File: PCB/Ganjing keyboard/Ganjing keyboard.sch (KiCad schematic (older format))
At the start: 166 parts, among them J1 AVR-ISP-6, J2 Conn_01x04, SW1 Rotary_Encoder_Switch, U1 ATmega32A-PU, Y1 Crystal

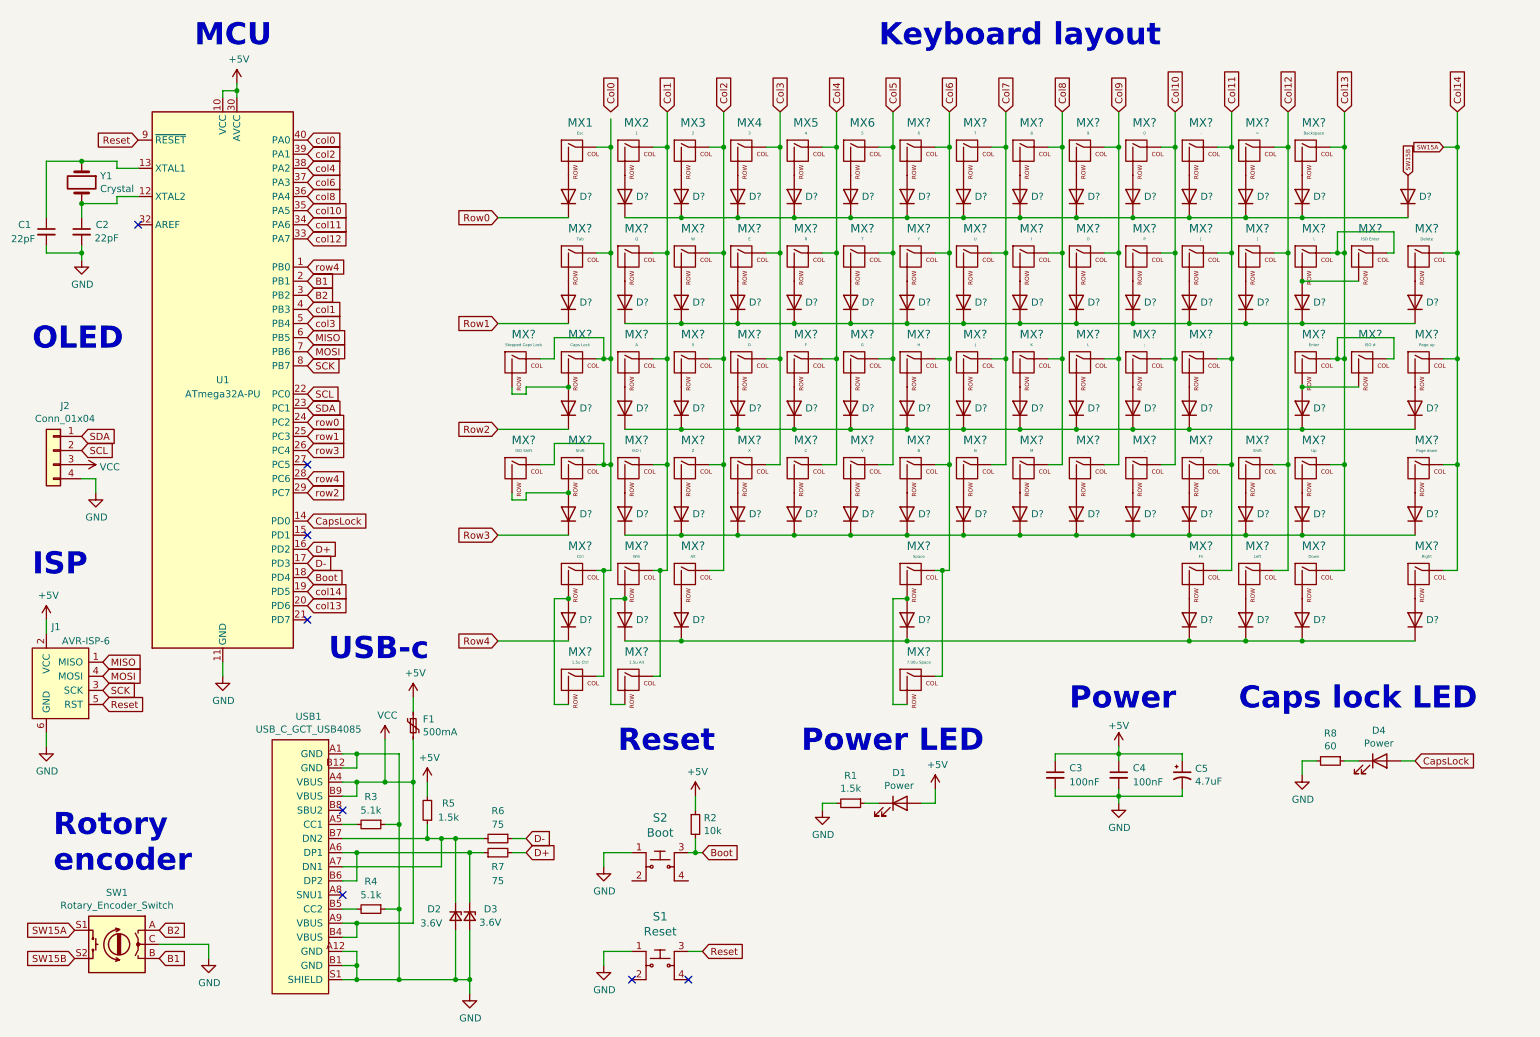
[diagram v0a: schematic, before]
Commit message: Updated schematic with reference values
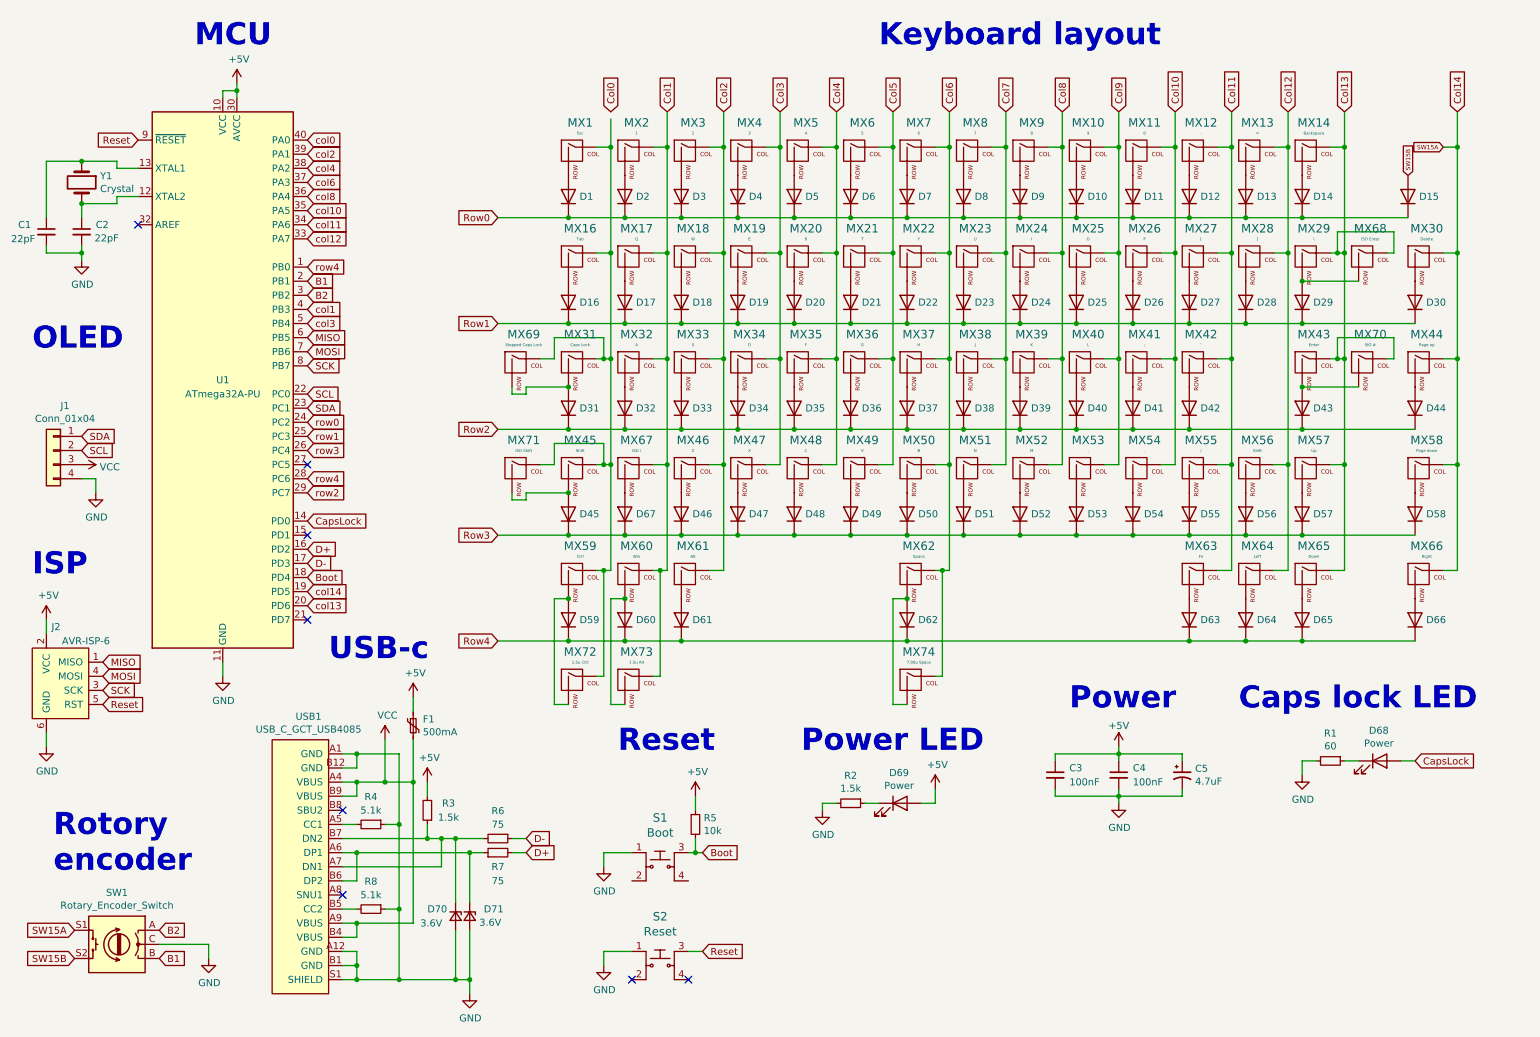
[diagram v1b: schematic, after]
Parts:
- gave numbers to parts that had none: 134
- renumbered D4 to D68, D1 to D69, D2 to D70, D3 to D71, J2 to J1, J1 to J2, R8 to R1, R1 to R2, R5 to R3, R3 to R4, R2 to R5, R4 to R8, S2 to S1, S1 to S2
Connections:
- net Row0: now also D10.1 (K), D11.1 (K), D12.1 (K), D13.1 (K), D14.1 (K), D15.1 (K), D2.1 (K), D3.1 (K), D4.1 (K), D5.1 (K), D6.1 (K), D7.1 (K), D8.1 (K), D9.1 (K)
- net Row1: now also D17.1 (K), D18.1 (K), D19.1 (K), D20.1 (K), D21.1 (K), D22.1 (K), D23.1 (K), D24.1 (K), D25.1 (K), D26.1 (K), D27.1 (K), D28.1 (K), D29.1 (K), D30.1 (K)
- net Row2: now also D32.1 (K), D33.1 (K), D34.1 (K), D35.1 (K), D36.1 (K), D37.1 (K), D38.1 (K), D39.1 (K), D40.1 (K), D41.1 (K), D42.1 (K), D43.1 (K), D44.1 (K)
- net Row3: now also D46.1 (K), D47.1 (K), D48.1 (K), D49.1 (K), D50.1 (K), D51.1 (K), D52.1 (K), D53.1 (K), D54.1 (K), D55.1 (K), D56.1 (K), D57.1 (K), D58.1 (K), D67.1 (K)
- net Row4: now also D60.1 (K), D61.1 (K), D62.1 (K), D63.1 (K), D64.1 (K), D65.1 (K), D66.1 (K)

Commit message: Added part numbers, links, and datasheets to all symbols, as well as changing the 60 ohm resistor to 62 ohm. All symbols now have associated footprints
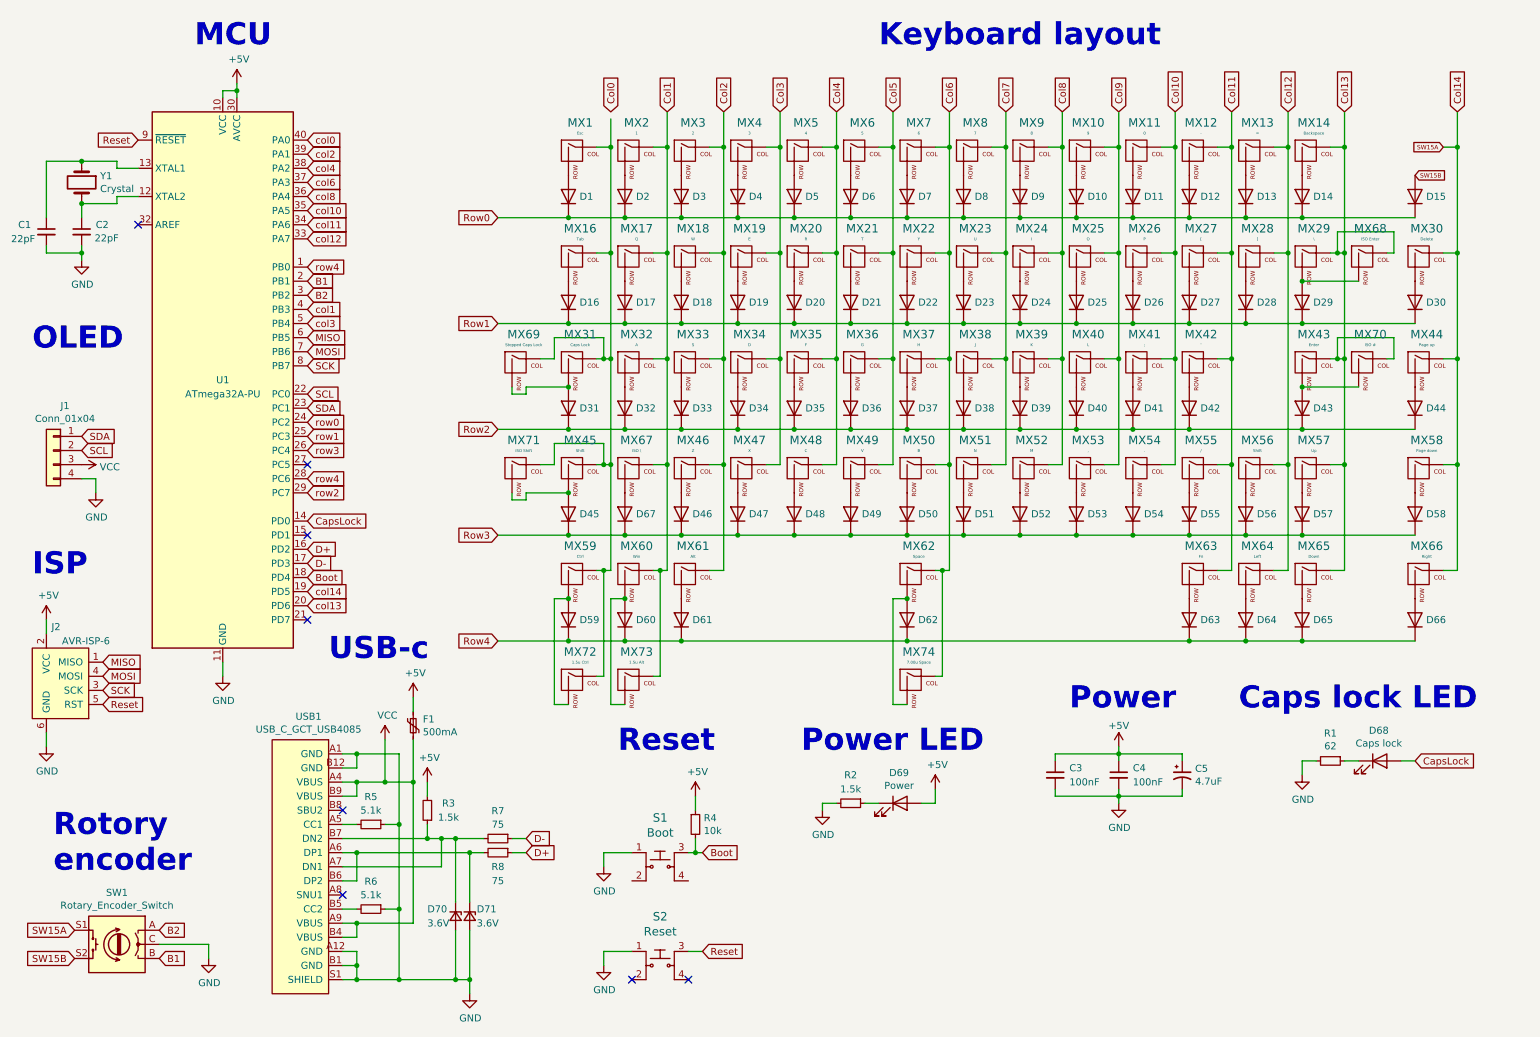
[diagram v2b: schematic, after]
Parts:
- removed R7: 75, symbol Device:R_Small
- added R6: 5.1k, Resistor_THT:R_Axial_DIN0204_L3.6mm_D1.6mm_P5.08mm_Horizontal, symbol Device:R_Small
- C1, C2: footprint (none) -> Keyboard:C_Disc_D3.0mm_W1.6mm_P2.50mm; Digikey # (none) -> 490-11879-ND; Digikey link (none) -> https://www.digikey.ca/en/products/detail/murata-electronic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
- C3, C4: footprint (none) -> Keyboard:C_Disc_D4.3mm_W1.9mm_P5.00mm; Digikey # (none) -> https://www.digikey.ca/en/products/detail/murata-electronic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; Digikey link (none) -> https://www.digikey.ca/en/products/detail/murata-electronic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
- C5: footprint (none) -> Keyboard:CP_Radial_D4.0mm_P1.50mm; Mouser # (none) -> 647-UMT1H4R7MDD1TP; Mouser link (none) -> https://www.mouser.com/ProductDetail/Nichicon/UMT1H4R7MDD1T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
- D1, D10, D11, D12, D13, D14, D15, D16, D17, D18, D19, D2, D20, D21, D22, D23, D24, D25, D26, D27, D28, D29, D3, D30, D31, D32, D33, D34, D35, D36, D37, D38, D39, D4, D40, D41, D42, D43, D44, D45, D46, D47, D48, D49, D5, D50, D51, D52, D53, D54, D55, D56, D57, D58, D59, D6, D60, D61, D62, D63, D64, D65, D66, D67, D7, D8, D9: footprint (none) -> Diode_THT:D_DO-35_SOD27_P5.08mm_Vertical_AnodeUp; Digikey # (none) -> 1N4148FSTR-ND; Digikey Link (none) -> https://www.digikey.ca/en/products/detail/on-semiconductor/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
- D68: value Power -> Caps lock; footprint (none) -> Keyboard:LED_D3.0mm; Digikey # (none) -> 160-1143-ND; Digikey link (none) -> https://www.digikey.ca/en/products/detail/lite-on-inc/ltl-4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
- D69: footprint (none) -> Keyboard:LED_D3.0mm; Digikey # (none) -> 160-1140-ND; Digikey link (none) -> https://www.digikey.ca/en/products/detail/lite-on-inc/ltl-4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
- D70, D71: footprint (none) -> Diode_THT:D_DO-35_SOD27_P5.08mm_Vertical_AnodeUp; Mouser # (none) -> 78-TZX3V6A; Mouser link (none) -> https://www.mouser.com/ProductDetail/Vishay-Semiconductors/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
- F1: footprint (none) -> Keyboard:polyfuse_5.1mm; Digikey # (none) -> MF-R050-ND; Digikey link (none) -> https://www.digikey.ca/en/products/detail/bourns-inc/mf-r05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
- J1: footprint (none) -> Keyboard:ssd1306 128x32 oled
- J2: footprint (none) -> Keyboard:AVR_ICSP_3x2; Digikey # (none) -> 609-4934-ND; Digikey link (none) -> https://www.digikey.ca/en/products/detail/amphenol-icc-fci/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
- MX1, MX10, MX11, MX12, MX13, MX17, MX18, MX19, MX2, MX20, MX21, MX22, MX23, MX24, MX25, MX26, MX27, MX28, MX3, MX30, MX32, MX33, MX34, MX35, MX36, MX37, MX38, MX39, MX4, MX40, MX41, MX42, MX44, MX46, MX47, MX48, MX49, MX5, MX50, MX51, MX52, MX53, MX54, MX55, MX57, MX58, MX6, MX63, MX64, MX65, MX66, MX67, MX7, MX70, MX8, MX9: footprint (none) -> MX_Only:MXOnly-1U-NoLED
- MX14: footprint (none) -> MX_Only:MXOnly-2U-NoLED
- MX16, MX29, MX72, MX73: footprint (none) -> MX_Only:MXOnly-1.5U-NoLED
- MX31, MX56: footprint (none) -> MX_Only:MXOnly-1.75U-NoLED
- MX43, MX45: footprint (none) -> MX_Only:MXOnly-2.25U-NoLED
- MX59, MX60, MX61, MX71: footprint (none) -> MX_Only:MXOnly-1.25U-NoLED
- MX62: footprint (none) -> MX_Only:MXOnly-6.25U-NoLED
- MX68: footprint (none) -> MX_Only:MXOnly-ISO_NoLED
- MX69: footprint (none) -> MX_Only:MXOnly-1.75U-Stepped-NoLED
- MX74: footprint (none) -> MX_Only:MXOnly-7U-NoLED
- R1: value 60 -> 62; footprint (none) -> Resistor_THT:R_Axial_DIN0204_L3.6mm_D1.6mm_P5.08mm_Horizontal; Mouser # (none) -> 603-MFR-25FTE52-62R; Mouser link (none) -> https://www.mouser.com/ProductDetail/Yageo/MFR-25FTE52-62R?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
- R2, R3: footprint (none) -> Resistor_THT:R_Axial_DIN0204_L3.6mm_D1.6mm_P5.08mm_Horizontal; Mouser # (none) -> 603-MFR-12FTF52-1K5; Mouser link (none) -> https://www.mouser.com/ProductDetail/Yageo/MFR-12FTF52-1K5?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
- R4: renamed from R5; footprint (none) -> Resistor_THT:R_Axial_DIN0204_L3.6mm_D1.6mm_P5.08mm_Horizontal; Field4 (none) -> 603-MFR-12FTF52-10K; Mouser link (none) -> https://www.mouser.com/ProductDetail/Yageo/MFR-12FTF52-10K?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
- R5: renamed from R4; footprint (none) -> Resistor_THT:R_Axial_DIN0204_L3.6mm_D1.6mm_P5.08mm_Horizontal; Mouser # (none) -> 603-MFR-12FTF52-5K1; Mouser link (none) -> https://www.mouser.com/ProductDetail/Yageo/MFR-12FTF52-5K1?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
- R7: renamed from R6; footprint (none) -> Resistor_THT:R_Axial_DIN0204_L3.6mm_D1.6mm_P5.08mm_Horizontal; Mouser # (none) -> 603-CFR-12JR-52-75R; Mouser link (none) -> https://www.mouser.com/ProductDetail/Yageo/CFR-12JR-52-75R?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
- R8: value 5.1k -> 75; footprint (none) -> Resistor_THT:R_Axial_DIN0204_L3.6mm_D1.6mm_P5.08mm_Horizontal; Mouser # (none) -> 603-CFR-12JR-52-75R; Mouser link (none) -> https://www.mouser.com/ProductDetail/Yageo/CFR-12JR-52-75R?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
- SW1: footprint (none) -> Rotary_Encoder:RotaryEncoder_Alps_EC11E-Switch_Vertical_H20mm; Mouser # (none) -> 688-EC11E183440C; Mouser link (none) -> https://www.mouser.com/ProductDetail/Alps-Alpine/EC11E18344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
- USB1: Digikey # (none) -> 2073-USB4085-GF-ATR-ND; Digikey link (none) -> https://www.digikey.ca/en/products/detail/gct/USB4085-GF-A/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
- Y1: footprint (none) -> Keyboard:Crystal_HC49-4H_Vertical; Mouser # (none) -> 815-ABL16000MHZB4YT; Mouser link (none) -> https://www.mouser.com/ProductDetail/ABRACON/ABL-16000MHz-B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
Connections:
- net D+: now also R8.1
- net GND: now also R6.1; no longer R8.1
- net at D71.1 (K), USB1.A6 (DP1), USB1.B6 (DP2): now also R8.2
- net at USB1.B5 (CC2): now also R6.2; no longer R8.2
